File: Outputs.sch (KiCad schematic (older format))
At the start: 21 parts

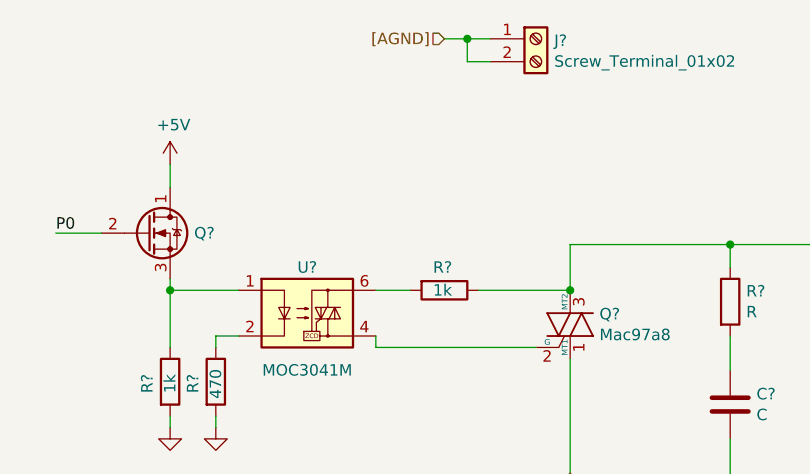
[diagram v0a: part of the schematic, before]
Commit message: MOC3043 no MOC3041
Cambiar componente
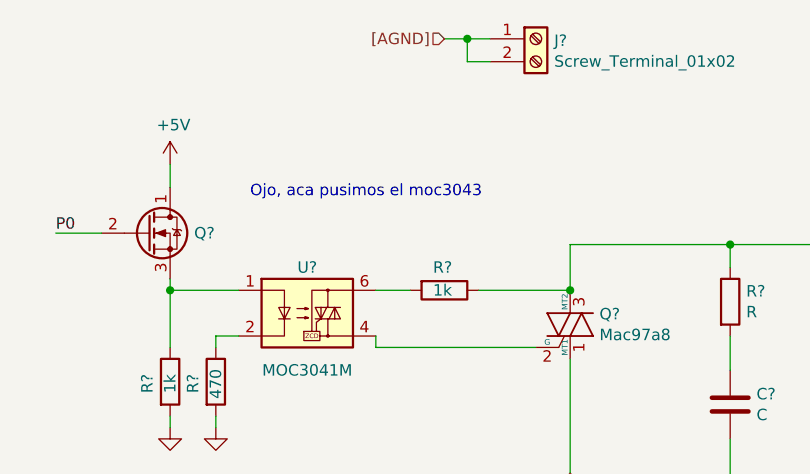
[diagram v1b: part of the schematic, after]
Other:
- note added: "Ojo, aca pusimos el moc3043"
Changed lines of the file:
@@
 Wire Wire Line
 	2900 4900 2900 5000
+Text Notes 7150 2250 0    50   ~ 0
+Ojo, aca pusimos el moc3043
 $EndSCHEMATC

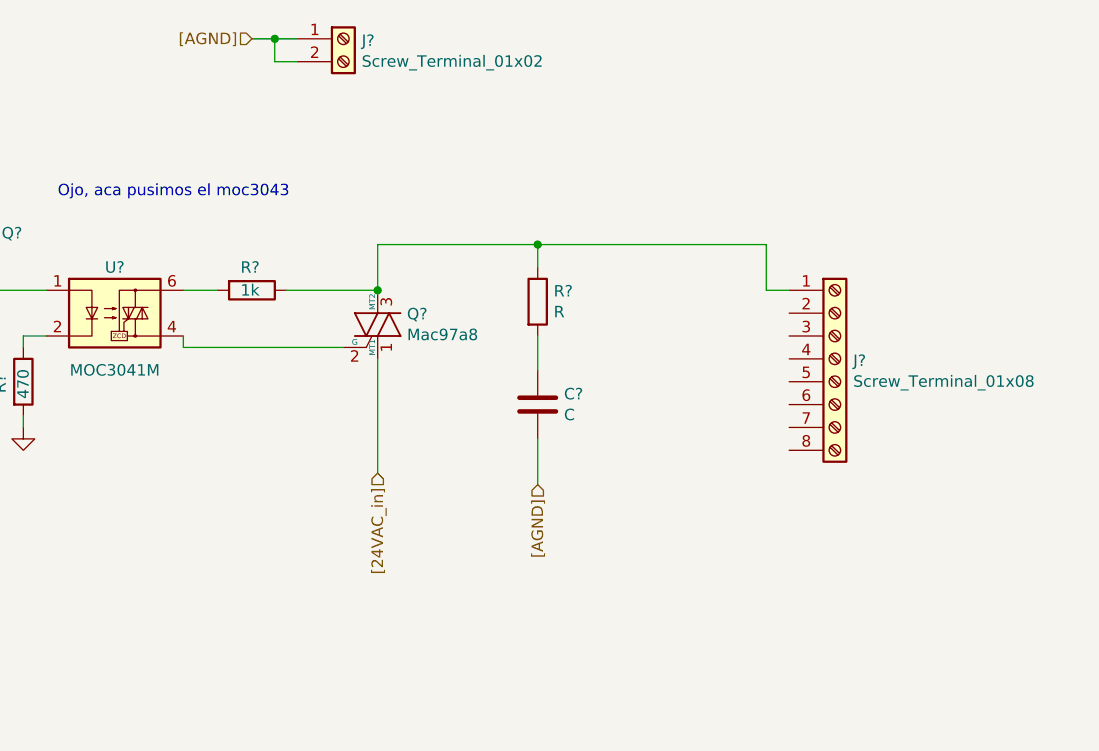
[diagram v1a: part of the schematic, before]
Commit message: Salidas está OK!
Dejo nota en el kicad "Text"
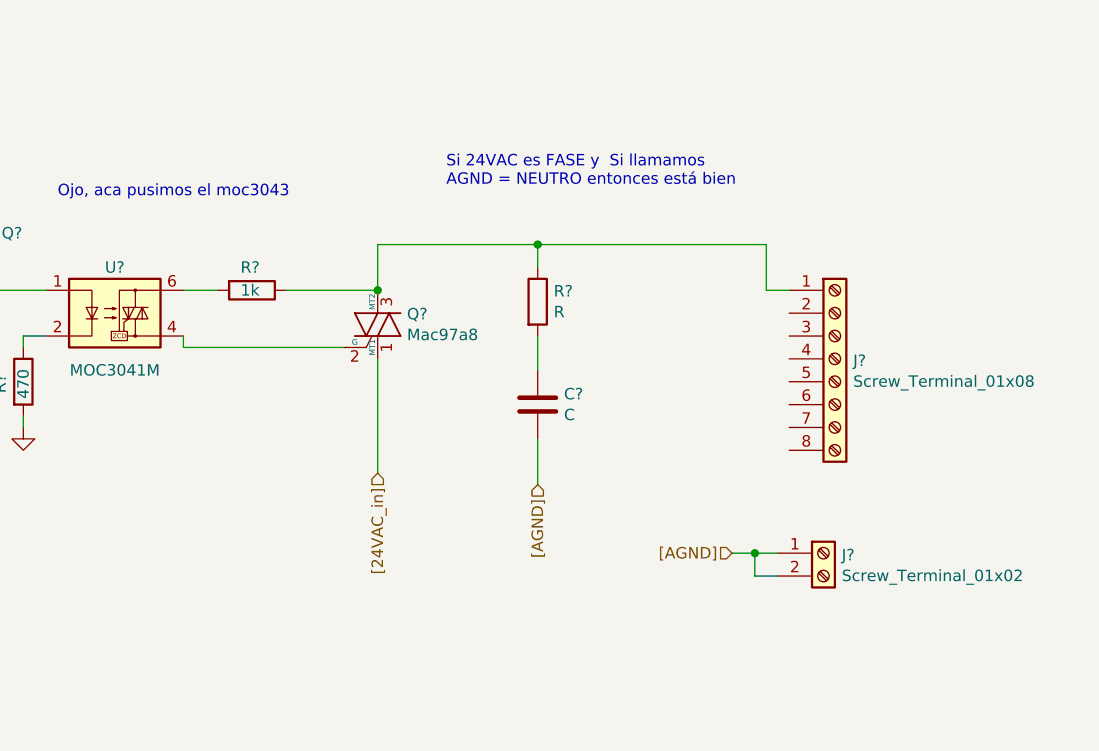
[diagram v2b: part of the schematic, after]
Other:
- note added: "Si 24VAC es FASE y Si llamamos \nAGND = NEUTRO entonces está bien"
- moved on the sheet: J?
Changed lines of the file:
@@
 L Connector:Screw_Terminal_01x02 J?
 U 1 1 61A00DC7
-P 8400 1550
-F 0 "J?" H 8480 1542 50  0000 L CNN
-F 1 "Screw_Terminal_01x02" H 8480 1451 50  0000 L CNN
-F 2 "" H 8400 1550 50  0001 C CNN
-F 3 "~" H 8400 1550 50  0001 C CNN
-	1    8400 1550
-	1    0    0    -1
-$EndComp
-Text HLabel 8000 1550 0    50   Input ~ 0
+P 10500 3800
+F 0 "J?" H 10580 3792 50  0000 L CNN
+F 1 "Screw_Terminal_01x02" H 10580 3701 50  0000 L CNN
+F 2 "" H 10500 3800 50  0001 C CNN
+F 3 "~" H 10500 3800 50  0001 C CNN
+	1    10500 3800
+	1    0    0    -1
+$EndComp
+Text HLabel 10100 3800 0    50   Input ~ 0
 [AGND]
 Wire Wire Line
-	8200 1550 8100 1550
-Wire Wire Line
-	8200 1650 8100 1650
-Wire Wire Line
-	8100 1650 8100 1550
-Connection ~ 8100 1550
-Wire Wire Line
-	8100 1550 8000 1550
+	10300 3800 10200 3800
+Wire Wire Line
+	10300 3900 10200 3900
+Wire Wire Line
+	10200 3900 10200 3800
+Connection ~ 10200 3800
+Wire Wire Line
+	10200 3800 10100 3800
 $Comp
 L Device:R R?
@@
 Text Notes 7150 2250 0    50   ~ 0
 Ojo, aca pusimos el moc3043
+Text Notes 8850 2200 0    50   ~ 0
+Si 24VAC es FASE y  Si llamamos \nAGND = NEUTRO entonces está bien
 $EndSCHEMATC
